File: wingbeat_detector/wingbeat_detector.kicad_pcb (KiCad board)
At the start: 2 copper layers, 36 x 18 mm, 52 parts, among them J1 USB_C_10137062-00021LF, J2 CONN_UMC_JACK_SMD, J3 CONN_UMC_JACK_SMD, J4 CONN_UMC_JACK_SMD, Q1 MOSFET-N-CH, U1 MAX865EUA+, U2 UAF42_SMA, U3 UAF42_SMA, U4 OPA381, U5 TSV630IQ1T, U6 LED_DRV_50mA

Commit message: Update courtyard for footprints
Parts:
- C13, J4, R15, R16, U2, U6: moved to B.Cu
- H1, H2, H3, H4: value MOUNTING_HOLE_2 -> VAL**
- moved C13 60.0 mm to (132.5, 114.0), turned to 180 degrees
- moved U6 40.7 mm to (131.5, 112.0)
- moved R16 38.7 mm to (134.5, 112.5), turned to 180 degrees
- moved R15 37.9 mm to (134.5, 113.5)
- moved J4 33.8 mm to (143.5, 106.5), turned to -90 degrees
- moved Q1 33.7 mm to (133.5, 111.5), turned to 0 degrees
- moved U2 26.4 mm to (153.0, 100.0)
- moved RV1 16.0 mm to (131.0, 122.5)

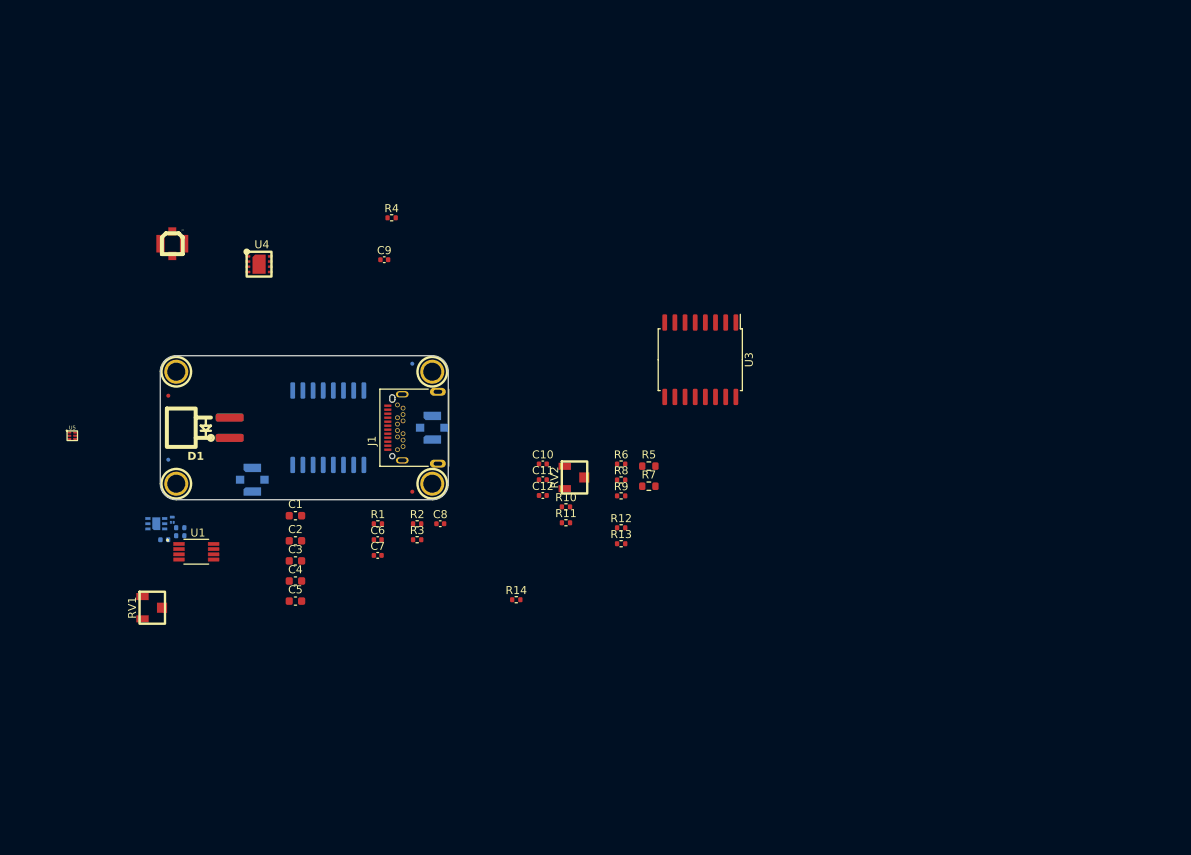
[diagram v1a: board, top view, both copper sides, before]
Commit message: Rearrange pcb footprints
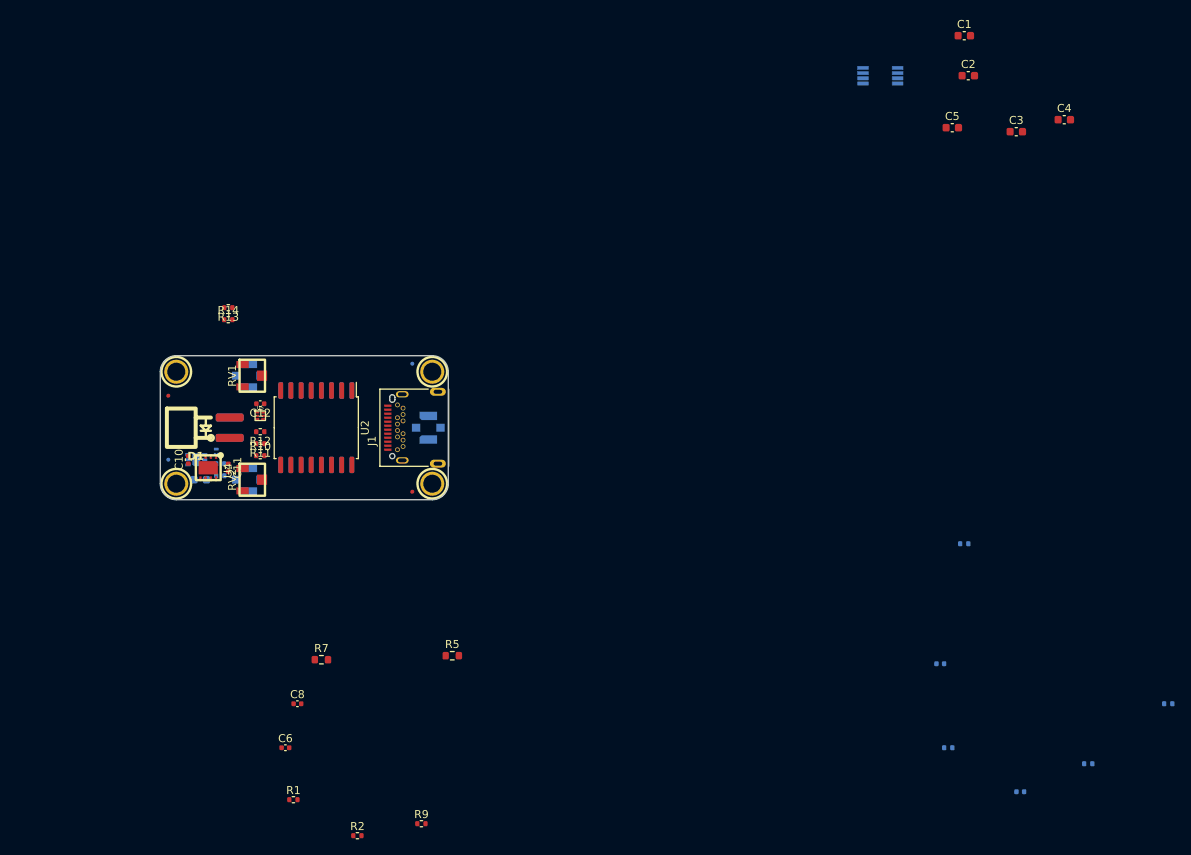
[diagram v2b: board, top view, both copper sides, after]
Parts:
- C13: value 0.1uF -> 4.7uF; footprint Janelia:C_0402_1005Metric -> Janelia:C_0603_1608Metric
- C7, C9, J3, R3, R4, R6, R8, U1, U3: moved to B.Cu
- H1, H2, H3, H4: value VAL** -> MOUNTING_HOLE_2
- U2: moved to F.Cu
- moved C4 112.1 mm to (245.0, 61.5)
- moved C3 104.9 mm to (239.0, 63.0)
- moved U1 104.2 mm to (222.0, 56.0), turned to 180 degrees
- moved C1 102.9 mm to (232.5, 51.0)
- moved C2 102.2 mm to (233.0, 56.0)
- moved C5 101.2 mm to (231.0, 62.5)
- moved C9 85.9 mm to (229.5, 129.5), turned to 180 degrees
- moved C7 85.6 mm to (239.5, 145.5), turned to 180 degrees
- moved R4 82.4 mm to (232.5, 114.5), turned to 180 degrees
- moved R8 73.9 mm to (258.0, 134.5), turned to 180 degrees
- moved R3 71.3 mm to (230.5, 140.0), turned to 180 degrees
- moved R6 69.4 mm to (248.0, 142.0), turned to 180 degrees
- moved R13 57.3 mm to (140.5, 85.0), turned to 180 degrees
- moved R14 50.2 mm to (140.5, 86.5)
- moved U3 48.7 mm to (151.5, 100.0), turned to 90 degrees
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
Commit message: Initial pcb component layout
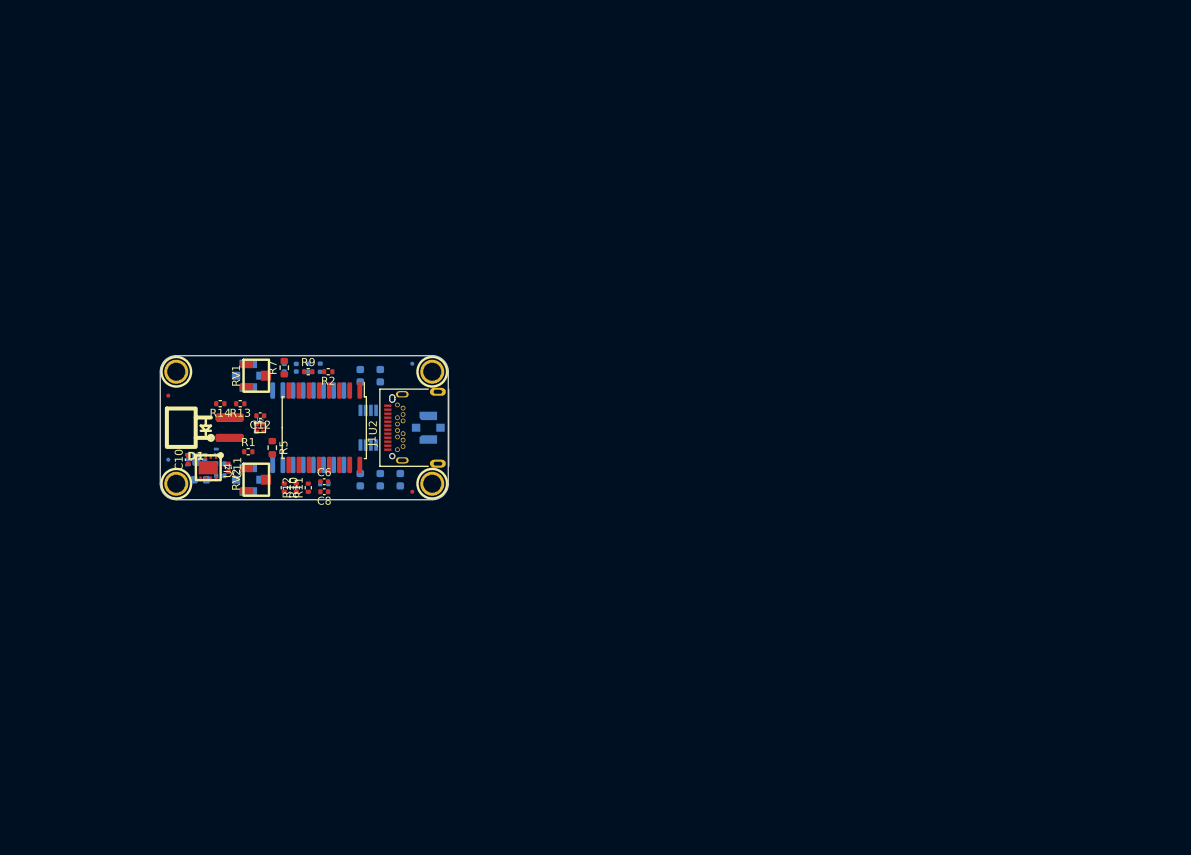
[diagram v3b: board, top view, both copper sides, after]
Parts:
- C1, C2, C3, C4, C5: moved to B.Cu
- moved R8 119.1 mm to (144.0, 100.0), turned to 90 degrees
- moved R6 108.0 mm to (152.0, 92.5), turned to 90 degrees
- moved C7 104.9 mm to (149.0, 92.5), turned to 90 degrees
- moved R3 93.0 mm to (150.5, 92.5), turned to 90 degrees
- moved C4 91.3 mm to (159.5, 93.5), turned to 90 degrees
- moved C3 90.6 mm to (159.5, 106.5), turned to -90 degrees
- moved C9 90.0 mm to (147.5, 92.5), turned to -90 degrees
- moved C2 87.1 mm to (162.0, 106.5), turned to -90 degrees
- moved C1 86.6 mm to (157.0, 93.5), turned to 90 degrees
- moved C5 86.1 mm to (157.0, 106.5), turned to 90 degrees
- moved R4 80.4 mm to (152.5, 107.0), turned to 0 degrees
- moved U1 77.7 mm to (158.0, 100.0), turned to 90 degrees
- moved R9 58.2 mm to (150.5, 93.0)
- moved R2 58.1 mm to (153.0, 93.0), turned to 180 degrees
- moved R1 43.9 mm to (143.0, 103.0)
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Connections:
- J3 pad 1: /photodiode/PHOTODIODE_BUFFERED -> /photodiode/PHOTODIODE_BUFFERED_SCALED
- R13 pad 1: Net-(U5--) -> /photodiode/PHOTODIODE_BUFFERED
- R13 pad 2: /photodiode/PHOTODIODE_BUFFERED -> /photodiode/PHOTODIODE_BUFFERED_SCALED
- R14 pad 1: /photodiode/PHOTODIODE_BUFFERED -> /photodiode/PHOTODIODE_BUFFERED_SCALED
- U5 pad 1: Net-(U5--) -> /photodiode/PHOTODIODE_BUFFERED
- U5 pad 3: Net-(U5--) -> /photodiode/PHOTODIODE_BUFFERED

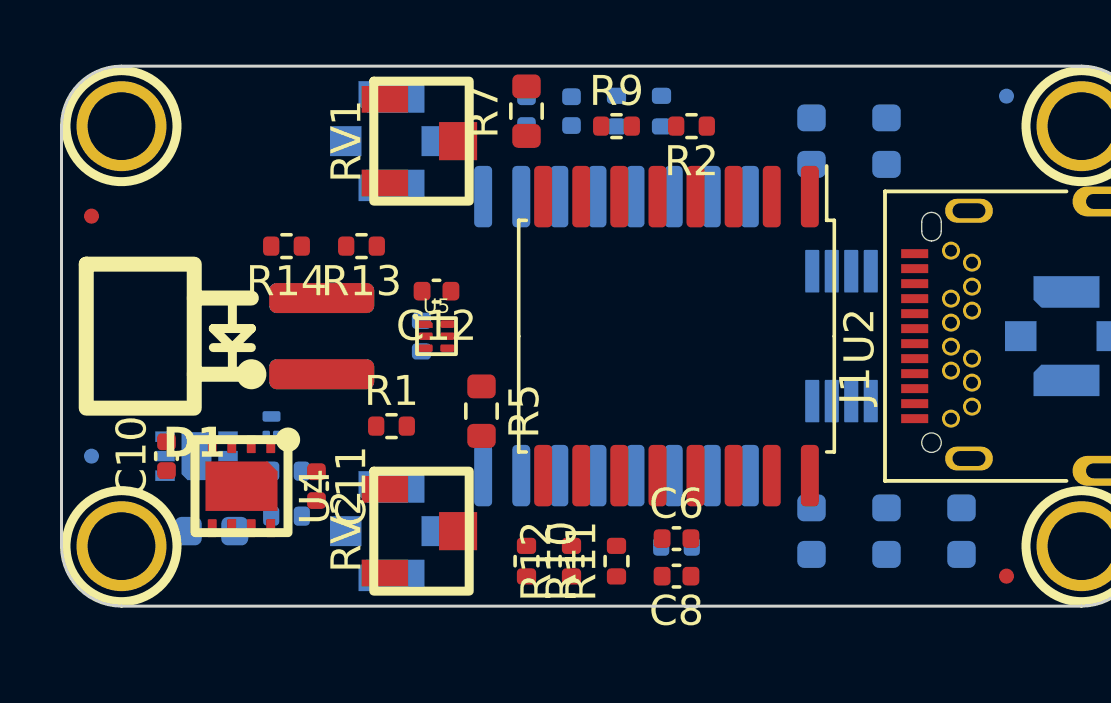
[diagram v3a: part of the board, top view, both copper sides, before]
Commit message: Move components after trying to route
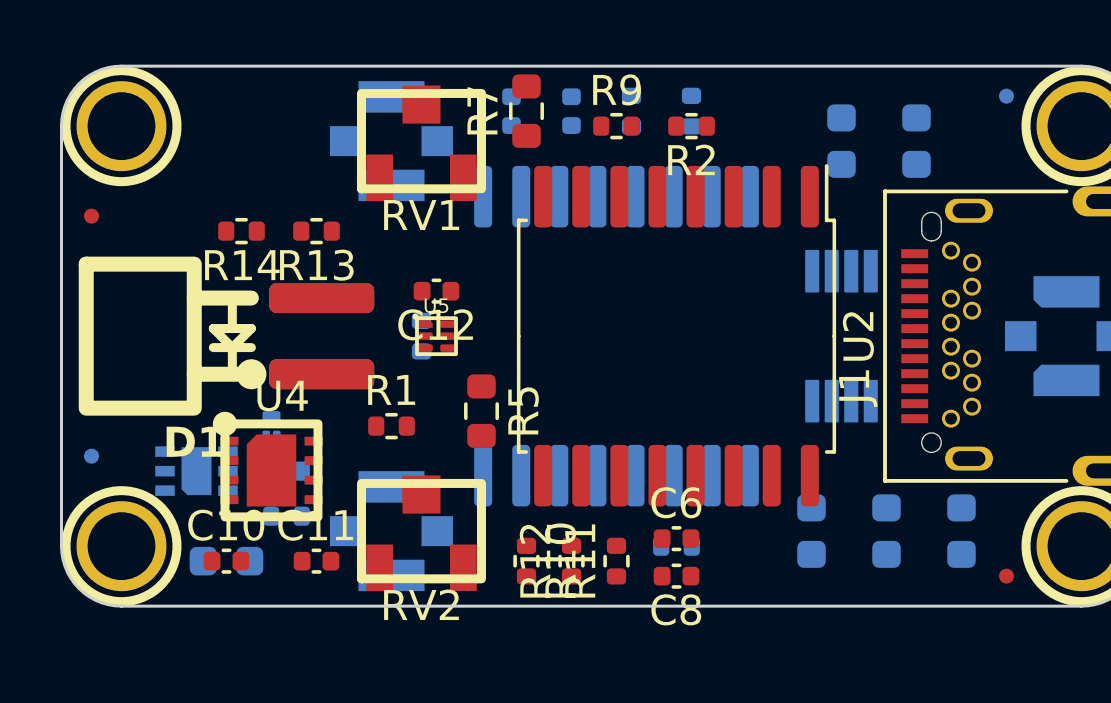
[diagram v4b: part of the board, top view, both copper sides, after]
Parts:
- moved C10 4.03 mm to (137.5, 107.5), turned to 0 degrees
- moved C11 2.50 mm to (140.5, 107.5), turned to 0 degrees
- moved R13 1.58 mm to (140.5, 96.5)
- moved R14 1.58 mm to (138.0, 96.5)
- moved U4 1.13 mm to (139.0, 104.5), turned to 0 degrees
- moved C13 1.12 mm to (137.5, 107.5)
- moved C1 1.00 mm to (158.0, 93.5)
- moved C4 1.00 mm to (160.5, 93.5)
- moved R6 1.00 mm to (153.0, 92.5)
- moved C9 0.50 mm to (147.0, 92.5)
- moved R3 0.50 mm to (151.0, 92.5)
- moved U6 0.50 mm to (136.5, 104.5)
- turned RV1 to 90 degrees
- turned RV2 to 90 degrees
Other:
- copper layers 2 -> 4

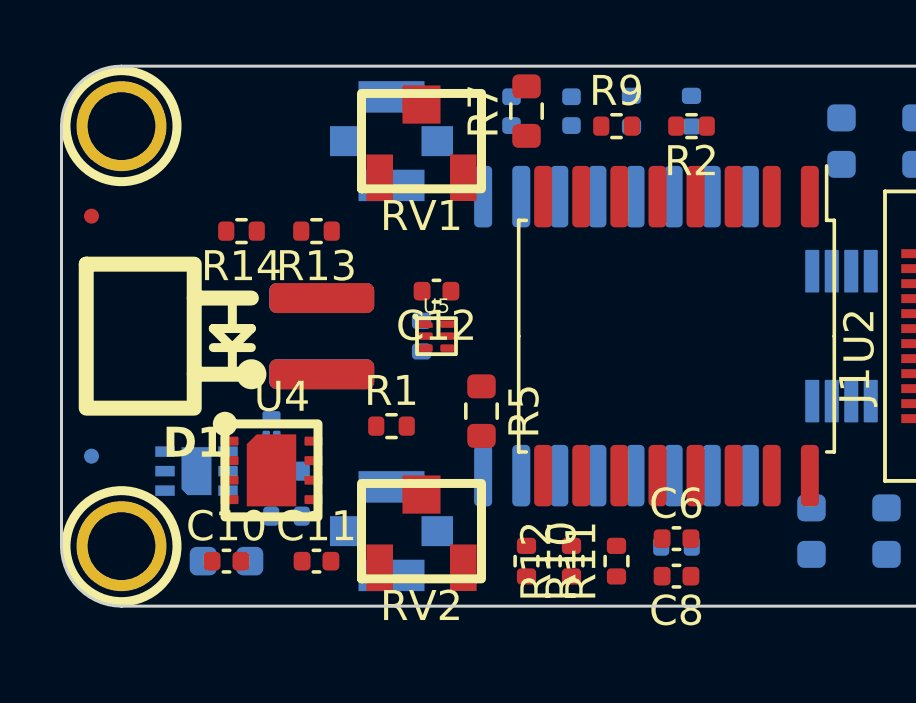
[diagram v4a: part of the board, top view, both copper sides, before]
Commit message: Move footprints and add some tracks
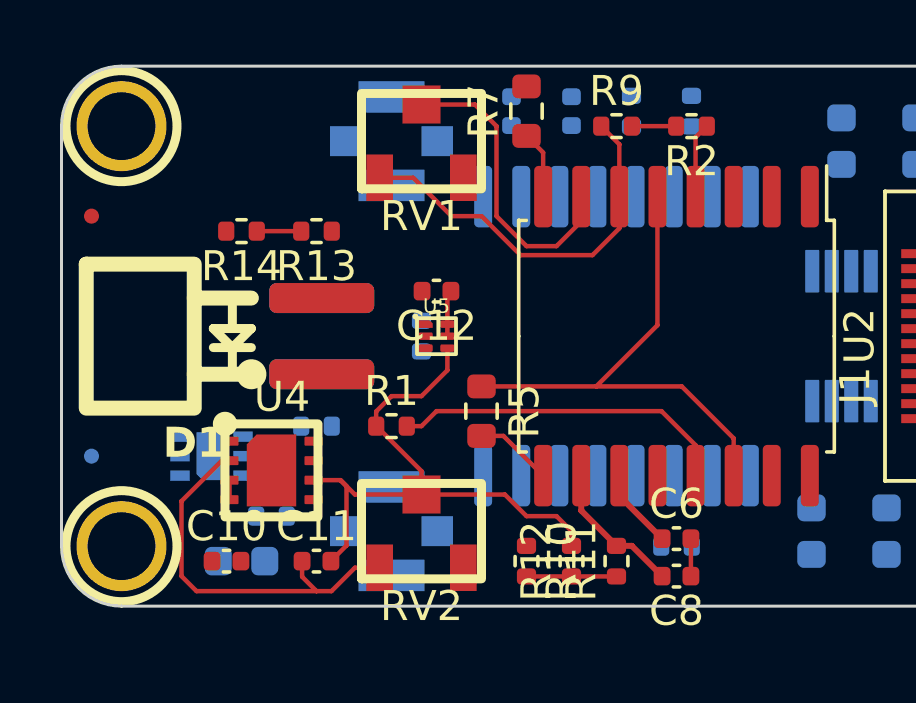
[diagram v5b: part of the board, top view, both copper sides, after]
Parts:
- H1, H2, H3, H4: value MOUNTING_HOLE_2 -> VAL**
- moved R16 1.80 mm to (140.5, 103.0), turned to 0 degrees
- moved Q1 1.58 mm to (139.5, 104.5)
- moved U6 0.71 mm to (137.0, 104.0)
- moved C13 0.50 mm to (138.0, 107.5), turned to 0 degrees
- moved R15 0.50 mm to (139.0, 106.0)
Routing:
- net /PHOTODIODE_RAW: track 0.00 -> 19.9 mm
- net /filter/HIGHPASS: track 0.00 -> 17.7 mm
- net Net-(U2-AAin-): track 0.00 -> 13.1 mm
- net Net-(D1-K): track 0.00 -> 13.0 mm
- net Net-(U2-Vin1): track 0.00 -> 11.3 mm
- net /filter/HIGHPASS_AMPLIFIED: track 0.00 -> 10.2 mm
- net /V10-: track 0.00 -> 4.77 mm
- net /GND: track 0.00 -> 3.59 mm
- net Net-(R10-Pad2): track 0.00 -> 3.00 mm
- net /V10+: track 0.00 -> 2.69 mm
- net Net-(U2-Fadj1): track 0.00 -> 2.60 mm
- net Net-(U2-Vin2): track 0.00 -> 2.51 mm
- net Net-(U2-BPVo): track 0.00 -> 2.25 mm
- net /V5+: track 0.00 -> 1.55 mm
- net /photodiode/PHOTODIODE_BUFFERED_SCALED: track 0.00 -> 1.48 mm

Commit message: Add more tracks
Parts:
- moved R2 1.00 mm to (154.0, 93.0)
- moved R9 1.00 mm to (151.5, 93.0)
- moved C7 0.50 mm to (148.5, 92.5)
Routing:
- net /GND: track 3.59 -> 46.7 mm, vias 0 -> 3
- net /filter/BANDPASS_BUFFERED: track 0.00 -> 27.3 mm
- net Net-(U2-Fadj2): track 0.00 -> 22.7 mm
- net /V5+: track 1.55 -> 18.4 mm, vias 0 -> 4
- net Net-(U3-Fadj1): track 0.00 -> 13.9 mm
- net Net-(U3-Fadj2): track 0.00 -> 13.7 mm
- net /filter/LOWPASS: track 0.00 -> 10.6 mm
- net Net-(D2-A): track 0.00 -> 9.75 mm
- net /power/C1+: track 0.00 -> 9.14 mm
- net /photodiode/PHOTODIODE_BUFFERED: track 0.00 -> 8.24 mm
- net /V10+: track 2.69 -> 9.56 mm
- net /power/C1-: track 0.00 -> 6.36 mm
- net /V10-: track 4.77 -> 10.8 mm
- net /power/C2-: track 0.00 -> 5.87 mm
- net Net-(D2-K): track 0.00 -> 5.76 mm
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
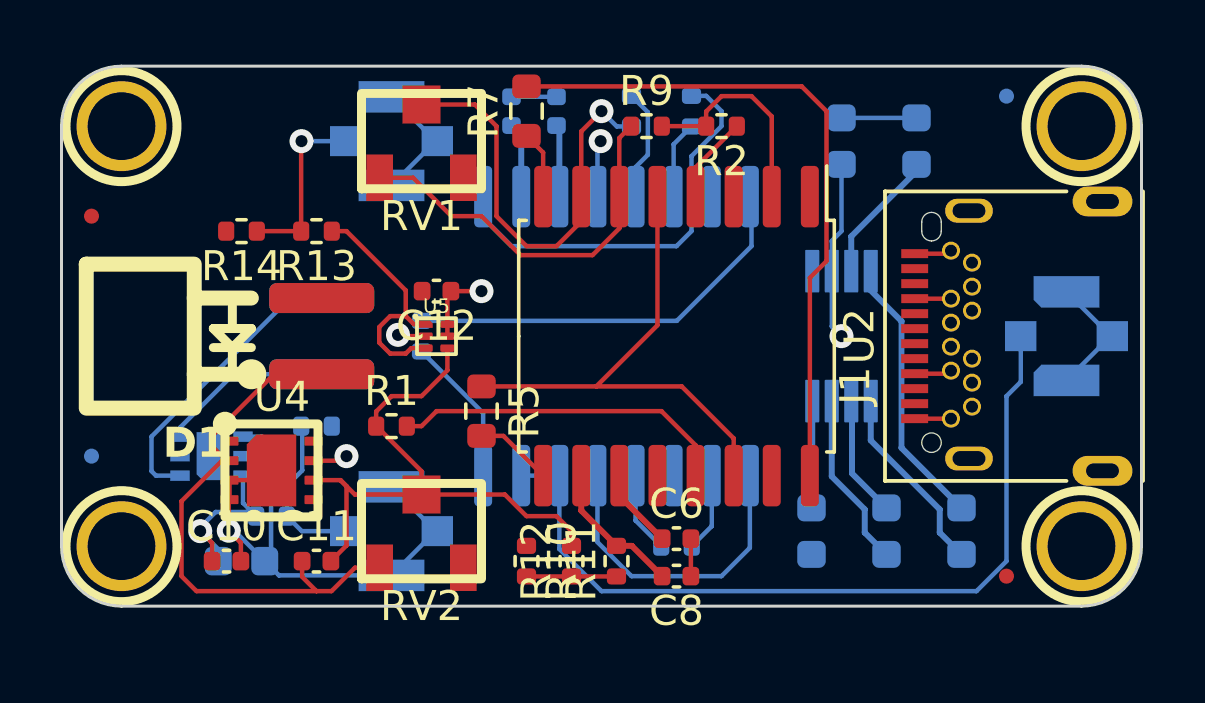
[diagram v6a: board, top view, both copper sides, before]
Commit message: Finished routing tracks with no errors
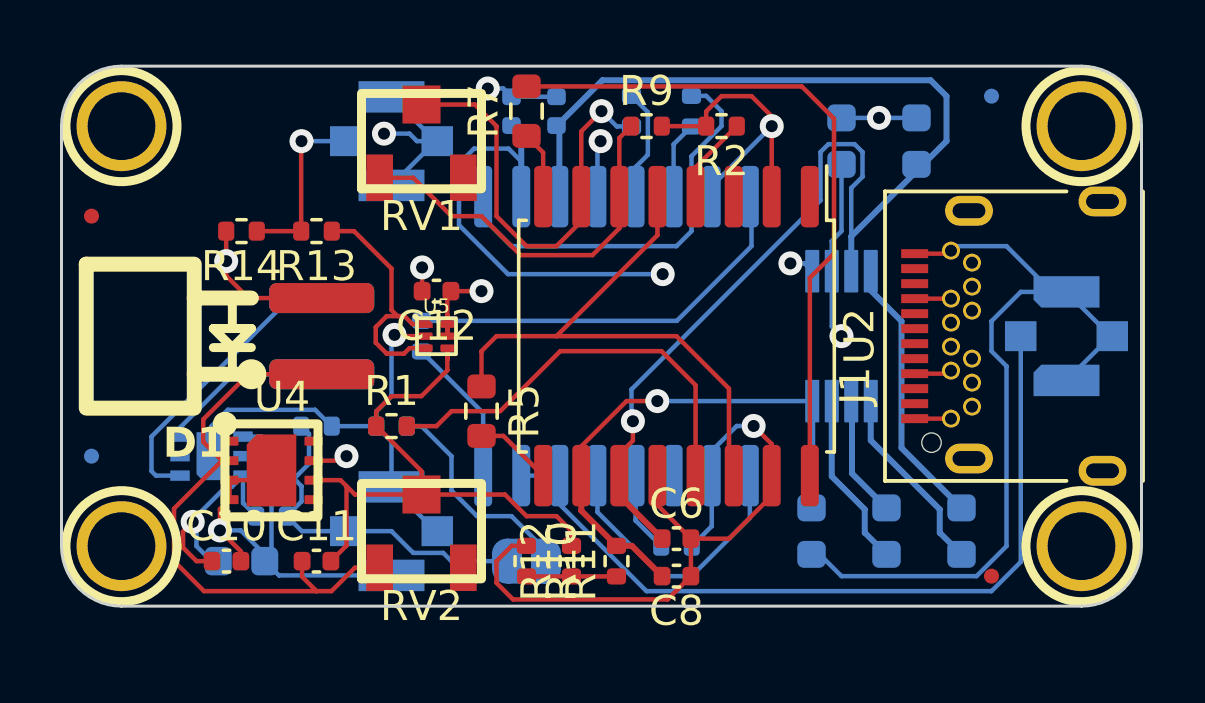
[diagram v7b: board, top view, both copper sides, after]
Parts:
- added JP1: SolderJumper_2_Open, Janelia:SolderJumper-2_P1.3mm_Open_RoundedPad1.0x1.5mm, B.Cu at (147.5, 107.5)
- added R17: 2k, Janelia:R_0402_1005Metric, B.Cu at (143.0, 103.0)
- H1, H2, H3, H4: value VAL** -> MOUNTING_HOLE_2
- moved FID2 0.50 mm to (163.0, 92.0)
- moved FID3 0.50 mm to (163.0, 108.0)
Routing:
- net /GND: track 46.7 -> 165.4 mm, vias 3 -> 11
- net /V5+: track 18.4 -> 54.7 mm
- net /V10+: track 9.56 -> 43.6 mm, vias 0 -> 1
- net /V10-: track 10.8 -> 36.1 mm, vias 0 -> 2
- net Net-(JP1-A): track 0.00 -> 7.03 mm
- net /led/LED_ENABLE: track 5.41 -> 11.7 mm
- net Net-(U2-Vin1): track 11.3 -> 14.1 mm
- net /filter/HIGHPASS: track 17.7 -> 19.3 mm
- net /filter/BANDPASS_BUFFERED: track 27.3 -> 25.8 mm
- net Net-(D1-K): track 18.6 -> 17.4 mm
- net /filter/LOWPASS: track 10.6 -> 9.39 mm
- net Net-(D2-A): track 9.75 -> 8.70 mm
- net /filter/HIGHPASS_AMPLIFIED: track 14.5 -> 13.7 mm
- net Net-(U3-Fadj1): track 13.9 -> 13.2 mm
- added copper zone on In1.Cu, net /GND
- added copper zone on In2.Cu, net /V5+
